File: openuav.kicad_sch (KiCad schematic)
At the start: 73 parts, among them J1 Conn_01x01, J10 Conn_01x01, J11 Conn_01x01, J12 Conn_01x01, J13 Conn_01x01, J14 Conn_01x01, J15 Conn_01x01, J16 Conn_01x01, J17 Conn_01x01, J18 Conn_01x01, J19 Conn_01x01, J2 Conn_01x01, J20 Conn_01x01, J21 Conn_01x01, J22 Conn_01x01, J23 Conn_01x01, J24 Conn_01x01, J25 Conn_01x01, J26 Conn_01x01, J27 Conn_01x01, J28 Conn_01x01, J29 Conn_01x01, J3 Conn_01x01, J30 Conn_01x01, J31 Conn_01x01, J32 Conn_01x01, J33 Conn_01x01, J34 Conn_01x01, J35 Conn_01x01, J36 Conn_01x01, J37 Conn_01x01, J4 Conn_01x01, J5 Conn_01x01, J6 Conn_01x01, J7 Conn_01x01, J8 Conn_01x01, J9 Conn_01x01, J99 USB_C_Receptacle_USB2.0, U1 STM32G431CBUx, U3 LSM6DSR, U4 LPS22HH, U5 TPS54202DDC, U6 W25N01GVZEIG, U7 XC6206P332MR

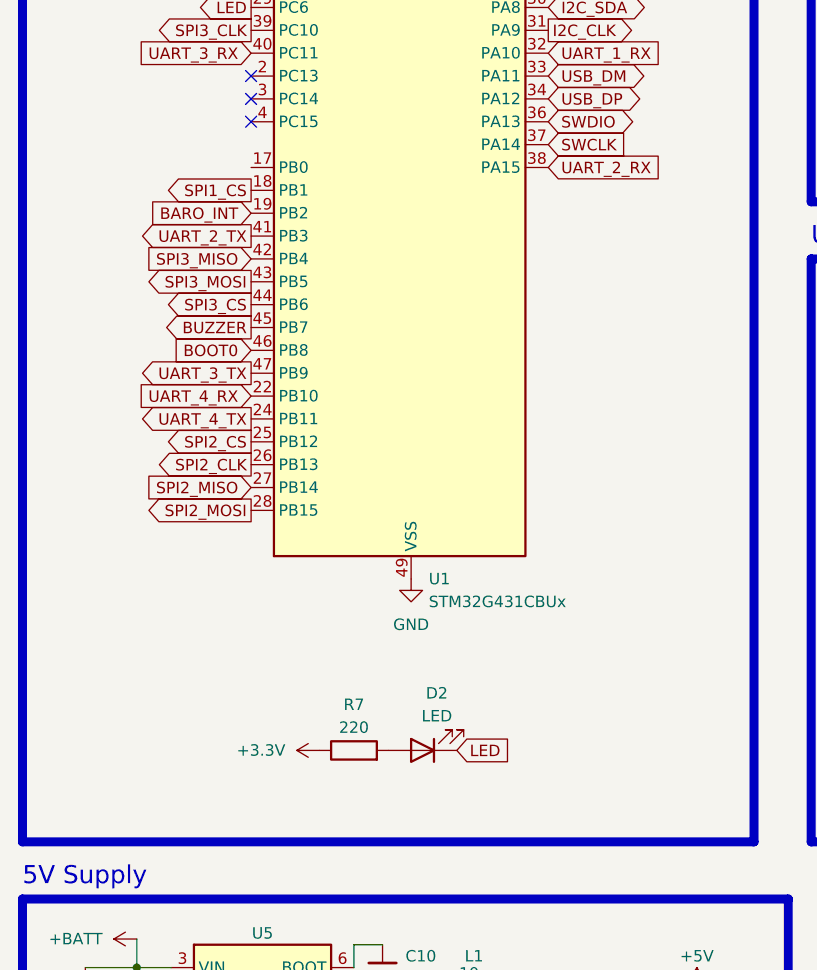
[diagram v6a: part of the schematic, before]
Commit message: update ioc file with all pins, add pulldown on boot0
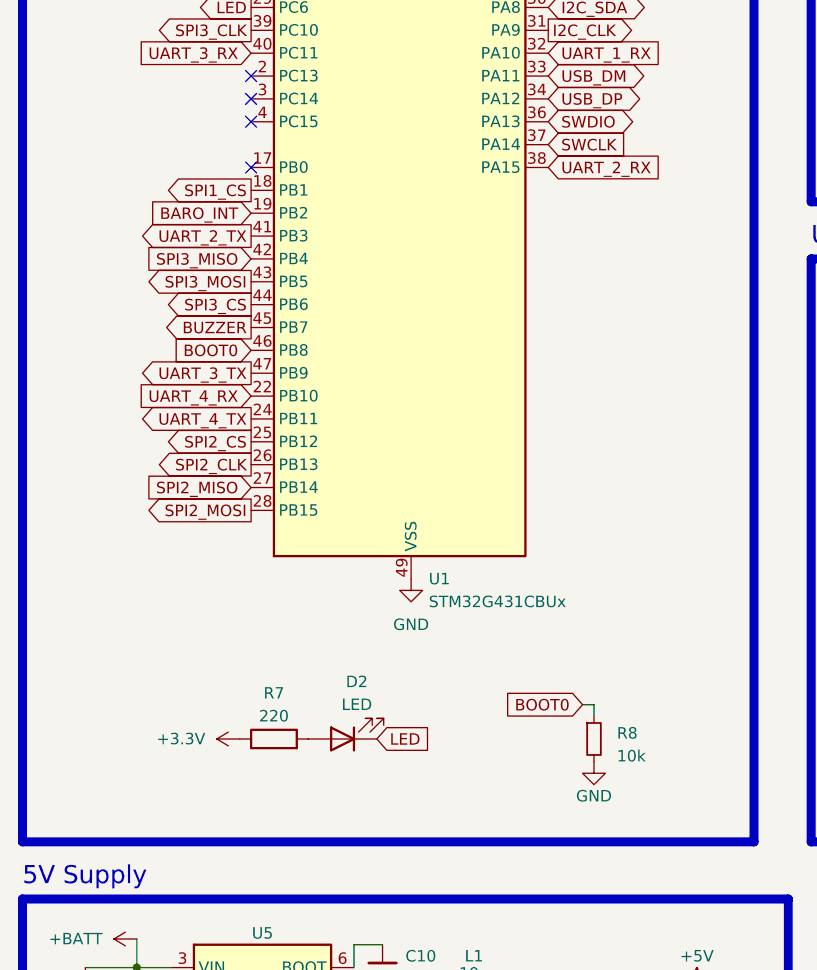
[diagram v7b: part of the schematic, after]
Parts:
- added R8: 10k, Resistor_SMD:R_0402_1005Metric, symbol Device:R_Small
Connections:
- net BOOT0: now also R8.1
- net GND: now also R8.2
- no-connect marks 12 -> 13
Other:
- moved on the sheet: D2, R7
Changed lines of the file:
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@@
   (no_connect (at 41.91 68.58))
   (no_connect (at 113.03 58.42))
+  (no_connect (at 41.91 76.2))
   (no_connect (at 121.92 101.6))
   (no_connect (at 178.435 115.57))
@@
     (stroke (width 0) (type default))
   )
+  (wire (pts (xy 80.01 135.89) (xy 80.01 137.16))
+    (stroke (width 0) (type default))
+  )
   (wire (pts (xy 259.334 175.26) (xy 269.494 175.26))
     (stroke (width 0) (type default))
@@
     (stroke (width 0) (type default))
   )
+  (wire (pts (xy 78.74 135.89) (xy 80.01 135.89))
+    (stroke (width 0) (type default))
+  )
   (wire (pts (xy 29.21 34.29) (xy 34.29 34.29))
     (stroke (width 0) (type default))
@@
     )
   )
-  (global_label "LED" (shape input) (at 64.77 140.97 0) (fields_autoplaced)
+  (global_label "LED" (shape input) (at 55.88 139.7 0) (fields_autoplaced)
     (effects (font (size 1.27 1.27)) (justify left))
-    (property "Intersheetrefs" "${INTERSHEET_REFS}" (at 71.1229 140.97 0)
+    (property "Intersheetrefs" "${INTERSHEET_REFS}" (at 62.2329 139.7 0)
       (effects (font (size 1.27 1.27)) (justify left) hide)
     )
@@
     )
   )
+  (global_label "BOOT0" (shape input) (at 78.74 135.89 180) (fields_autoplaced)
+    (effects (font (size 1.27 1.27)) (justify right))
+    (property "Intersheetrefs" "${INTERSHEET_REFS}" (at 69.7261 135.89 0)
+      (effects (font (size 1.27 1.27)) (justify right) hide)
+    )
+  )
   (global_label "SPI2_MOSI" (shape output) (at 41.91 114.3 180) (fields_autoplaced)
     (effects (font (size 1.27 1.27)) (justify right))
@@
     )
   )
+  (symbol (lib_id "Device:R_Small") (at 80.01 139.7 0) (unit 1)
+    (in_bom yes) (on_board yes) (dnp no) (fields_autoplaced)
+    (property "Reference" "R8" (at 82.55 139.065 0)
+      (effects (font (size 1.27 1.27)) (justify left))
+    )
+    (property "Value" "10k" (at 82.55 141.605 0)
+      (effects (font (size 1.27 1.27)) (justify left))
+    )
+    (property "Footprint" "Resistor_SMD:R_0402_1005Metric" (at 80.01 139.7 0)
+      (effects (font (size 1.27 1.27)) hide)
+    )
+    (property "Datasheet" "~" (at 80.01 139.7 0)
+      (effects (font (size 1.27 1.27)) hide)
+    )
+    (property "LCSC" "C17414" (at 80.01 139.7 0)
+      (effects (font (size 1.27 1.27)) hide)
+    )
+    (pin "1")
+    (pin "2")
+    (instances
+      (project "openuav"
+        (path "/e63e39d7-6ac0-4ffd-8aa3-1841a4541b55"
+          (reference "R8") (unit 1)
+        )
+      )
+    )
+  )
   (symbol (lib_id "power:GND") (at 59.69 121.92 0) (unit 1)
     (in_bom yes) (on_board yes) (dnp no) (fields_autoplaced)
@@
     )
   )
-  (symbol (lib_id "power:+3.3V") (at 49.53 140.97 90) (unit 1)
+  (symbol (lib_id "power:+3.3V") (at 40.64 139.7 90) (unit 1)
     (in_bom yes) (on_board yes) (dnp no)
-    (property "Reference" "#PWR023" (at 53.34 140.97 0)
+    (property "Reference" "#PWR023" (at 44.45 139.7 0)
       (effects (font (size 1.27 1.27)) hide)
     )
-    (property "Value" "+3.3V" (at 45.72 140.97 90)
+    (property "Value" "+3.3V" (at 36.83 139.7 90)
       (effects (font (size 1.27 1.27)) (justify left))
     )
-    (property "Footprint" "" (at 49.53 140.97 0)
+    (property "Footprint" "" (at 40.64 139.7 0)
       (effects (font (size 1.27 1.27)) hide)
     )
-    (property "Datasheet" "" (at 49.53 140.97 0)
+    (property "Datasheet" "" (at 40.64 139.7 0)
       (effects (font (size 1.27 1.27)) hide)
     )
@@
     )
   )
+  (symbol (lib_id "power:GND") (at 80.01 142.24 0) (unit 1)
+    (in_bom yes) (on_board yes) (dnp no)
+    (property "Reference" "#PWR039" (at 80.01 148.59 0)
+      (effects (font (size 1.27 1.27)) hide)
+    )
+    (property "Value" "GND" (at 80.01 146.05 0)
+      (effects (font (size 1.27 1.27)))
+    )
+    (property "Footprint" "" (at 80.01 142.24 0)
+      (effects (font (size 1.27 1.27)) hide)
+    )
+    (property "Datasheet" "" (at 80.01 142.24 0)
+      (effects (font (size 1.27 1.27)) hide)
+    )
+    (pin "1")
+    (instances
+      (project "openuav"
+        (path "/e63e39d7-6ac0-4ffd-8aa3-1841a4541b55"
+          (reference "#PWR039") (unit 1)
+        )
+      )
+    )
+  )
   (symbol (lib_id "Mechanical:MountingHole") (at 257.81 192.532 0) (unit 1)
     (in_bom yes) (on_board yes) (dnp no)
@@
     )
   )
-  (symbol (lib_id "Device:LED") (at 60.96 140.97 180) (unit 1)
+  (symbol (lib_id "Device:LED") (at 52.07 139.7 180) (unit 1)
     (in_bom yes) (on_board yes) (dnp no) (fields_autoplaced)
-    (property "Reference" "D2" (at 62.5475 134.62 0)
+    (property "Reference" "D2" (at 53.6575 133.35 0)
       (effects (font (size 1.27 1.27)))
     )
-    (property "Value" "LED" (at 62.5475 137.16 0)
+    (property "Value" "LED" (at 53.6575 135.89 0)
       (effects (font (size 1.27 1.27)))
     )
-    (property "Footprint" "LED_SMD:LED_0603_1608Metric" (at 60.96 140.97 0)
+    (property "Footprint" "LED_SMD:LED_0603_1608Metric" (at 52.07 139.7 0)
       (effects (font (size 1.27 1.27)) hide)
     )
-    (property "Datasheet" "~" (at 60.96 140.97 0)
+    (property "Datasheet" "~" (at 52.07 139.7 0)
       (effects (font (size 1.27 1.27)) hide)
     )
-    (property "LCSC" "C72041" (at 60.96 140.97 0)
+    (property "LCSC" "C72041" (at 52.07 139.7 0)
       (effects (font (size 1.27 1.27)) hide)
     )
@@
     )
   )
-  (symbol (lib_id "Device:R") (at 53.34 140.97 90) (unit 1)
+  (symbol (lib_id "Device:R") (at 44.45 139.7 90) (unit 1)
     (in_bom yes) (on_board yes) (dnp no) (fields_autoplaced)
-    (property "Reference" "R7" (at 53.34 135.89 90)
+    (property "Reference" "R7" (at 44.45 134.62 90)
       (effects (font (size 1.27 1.27)))
     )
-    (property "Value" "220" (at 53.34 138.43 90)
+    (property "Value" "220" (at 44.45 137.16 90)
       (effects (font (size 1.27 1.27)))
     )
-    (property "Footprint" "Resistor_SMD:R_0805_2012Metric" (at 53.34 142.748 90)
+    (property "Footprint" "Resistor_SMD:R_0805_2012Metric" (at 44.45 141.478 90)
       (effects (font (size 1.27 1.27)) hide)
     )
-    (property "Datasheet" "~" (at 53.34 140.97 0)
+    (property "Datasheet" "~" (at 44.45 139.7 0)
       (effects (font (size 1.27 1.27)) hide)
     )
-    (property "LCSC" "C17557" (at 53.34 140.97 90)
+    (property "LCSC" "C17557" (at 44.45 139.7 90)
       (effects (font (size 1.27 1.27)) hide)
     )

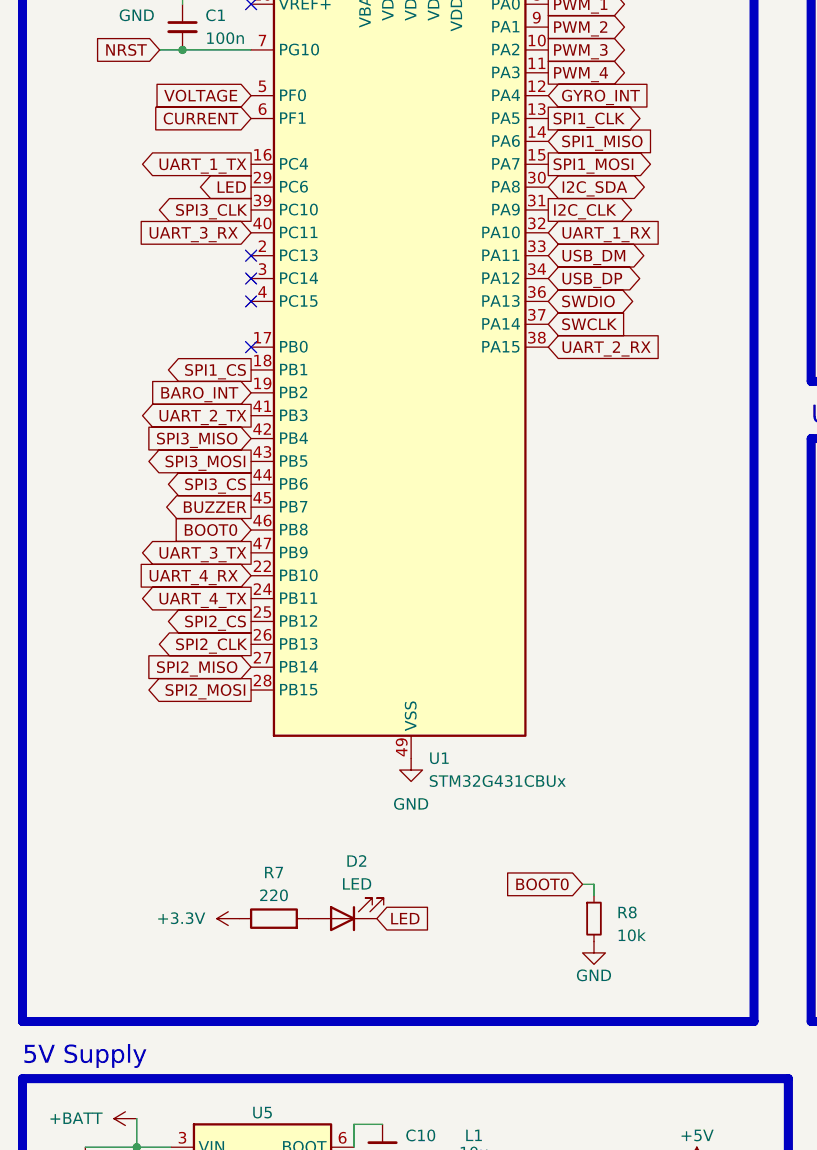
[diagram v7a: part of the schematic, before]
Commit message: add note about TT pin
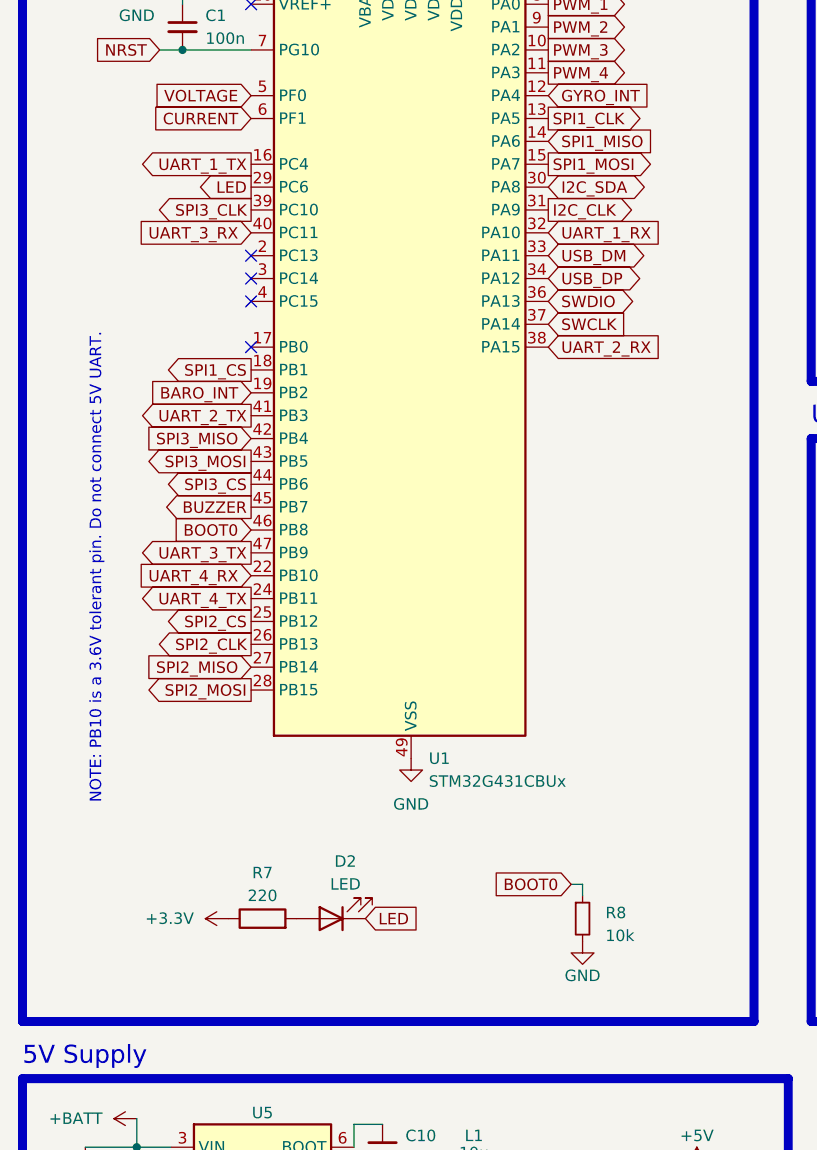
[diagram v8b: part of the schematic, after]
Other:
- note added: "NOTE: PB10 is a 3.6V tolerant pin. Do not connect 5V UART."
- moved on the sheet: D2, R7, R8
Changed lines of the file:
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@@
     (stroke (width 0) (type default))
   )
-  (wire (pts (xy 80.01 135.89) (xy 80.01 137.16))
+  (wire (pts (xy 78.74 135.89) (xy 78.74 137.16))
     (stroke (width 0) (type default))
   )
@@
     (stroke (width 0) (type default))
   )
-  (wire (pts (xy 78.74 135.89) (xy 80.01 135.89))
+  (wire (pts (xy 77.47 135.89) (xy 78.74 135.89))
     (stroke (width 0) (type default))
   )
@@
     (effects (font (size 2 2)) (justify left bottom))
   )
+  (text "NOTE: PB10 is a 3.6V tolerant pin. Do not connect 5V UART."
+    (at 25.4 127 90)
+    (effects (font (size 1.27 1.27)) (justify left bottom))
+  )
   (text "Flash" (at 161.29 85.09 0)
     (effects (font (size 2 2)) (justify left bottom))
@@
     )
   )
-  (global_label "LED" (shape input) (at 55.88 139.7 0) (fields_autoplaced)
+  (global_label "LED" (shape input) (at 54.61 139.7 0) (fields_autoplaced)
     (effects (font (size 1.27 1.27)) (justify left))
-    (property "Intersheetrefs" "${INTERSHEET_REFS}" (at 62.2329 139.7 0)
+    (property "Intersheetrefs" "${INTERSHEET_REFS}" (at 60.9629 139.7 0)
       (effects (font (size 1.27 1.27)) (justify left) hide)
     )
@@
     )
   )
-  (global_label "BOOT0" (shape input) (at 78.74 135.89 180) (fields_autoplaced)
+  (global_label "BOOT0" (shape input) (at 77.47 135.89 180) (fields_autoplaced)
     (effects (font (size 1.27 1.27)) (justify right))
-    (property "Intersheetrefs" "${INTERSHEET_REFS}" (at 69.7261 135.89 0)
+    (property "Intersheetrefs" "${INTERSHEET_REFS}" (at 68.4561 135.89 0)
       (effects (font (size 1.27 1.27)) (justify right) hide)
     )
@@
     )
   )
-  (symbol (lib_id "Device:R_Small") (at 80.01 139.7 0) (unit 1)
+  (symbol (lib_id "Device:R_Small") (at 78.74 139.7 0) (unit 1)
     (in_bom yes) (on_board yes) (dnp no) (fields_autoplaced)
-    (property "Reference" "R8" (at 82.55 139.065 0)
+    (property "Reference" "R8" (at 81.28 139.065 0)
       (effects (font (size 1.27 1.27)) (justify left))
     )
-    (property "Value" "10k" (at 82.55 141.605 0)
+    (property "Value" "10k" (at 81.28 141.605 0)
       (effects (font (size 1.27 1.27)) (justify left))
     )
-    (property "Footprint" "Resistor_SMD:R_0402_1005Metric" (at 80.01 139.7 0)
+    (property "Footprint" "Resistor_SMD:R_0402_1005Metric" (at 78.74 139.7 0)
       (effects (font (size 1.27 1.27)) hide)
     )
-    (property "Datasheet" "~" (at 80.01 139.7 0)
+    (property "Datasheet" "~" (at 78.74 139.7 0)
       (effects (font (size 1.27 1.27)) hide)
     )
-    (property "LCSC" "C17414" (at 80.01 139.7 0)
+    (property "LCSC" "C17414" (at 78.74 139.7 0)
       (effects (font (size 1.27 1.27)) hide)
     )
@@
     )
   )
-  (symbol (lib_id "power:+3.3V") (at 40.64 139.7 90) (unit 1)
+  (symbol (lib_id "power:+3.3V") (at 39.37 139.7 90) (unit 1)
     (in_bom yes) (on_board yes) (dnp no)
-    (property "Reference" "#PWR023" (at 44.45 139.7 0)
+    (property "Reference" "#PWR023" (at 43.18 139.7 0)
       (effects (font (size 1.27 1.27)) hide)
     )
-    (property "Value" "+3.3V" (at 36.83 139.7 90)
+    (property "Value" "+3.3V" (at 35.56 139.7 90)
       (effects (font (size 1.27 1.27)) (justify left))
     )
-    (property "Footprint" "" (at 40.64 139.7 0)
+    (property "Footprint" "" (at 39.37 139.7 0)
       (effects (font (size 1.27 1.27)) hide)
     )
-    (property "Datasheet" "" (at 40.64 139.7 0)
+    (property "Datasheet" "" (at 39.37 139.7 0)
       (effects (font (size 1.27 1.27)) hide)
     )
@@
     )
   )
-  (symbol (lib_id "power:GND") (at 80.01 142.24 0) (unit 1)
+  (symbol (lib_id "power:GND") (at 78.74 142.24 0) (unit 1)
     (in_bom yes) (on_board yes) (dnp no)
-    (property "Reference" "#PWR039" (at 80.01 148.59 0)
+    (property "Reference" "#PWR039" (at 78.74 148.59 0)
       (effects (font (size 1.27 1.27)) hide)
     )
-    (property "Value" "GND" (at 80.01 146.05 0)
+    (property "Value" "GND" (at 78.74 146.05 0)
       (effects (font (size 1.27 1.27)))
     )
-    (property "Footprint" "" (at 80.01 142.24 0)
+    (property "Footprint" "" (at 78.74 142.24 0)
       (effects (font (size 1.27 1.27)) hide)
     )
-    (property "Datasheet" "" (at 80.01 142.24 0)
+    (property "Datasheet" "" (at 78.74 142.24 0)
       (effects (font (size 1.27 1.27)) hide)
     )
@@
     )
   )
-  (symbol (lib_id "Device:LED") (at 52.07 139.7 180) (unit 1)
+  (symbol (lib_id "Device:LED") (at 50.8 139.7 180) (unit 1)
     (in_bom yes) (on_board yes) (dnp no) (fields_autoplaced)
-    (property "Reference" "D2" (at 53.6575 133.35 0)
+    (property "Reference" "D2" (at 52.3875 133.35 0)
       (effects (font (size 1.27 1.27)))
     )
-    (property "Value" "LED" (at 53.6575 135.89 0)
+    (property "Value" "LED" (at 52.3875 135.89 0)
       (effects (font (size 1.27 1.27)))
     )
-    (property "Footprint" "LED_SMD:LED_0603_1608Metric" (at 52.07 139.7 0)
+    (property "Footprint" "LED_SMD:LED_0603_1608Metric" (at 50.8 139.7 0)
       (effects (font (size 1.27 1.27)) hide)
     )
-    (property "Datasheet" "~" (at 52.07 139.7 0)
+    (property "Datasheet" "~" (at 50.8 139.7 0)
       (effects (font (size 1.27 1.27)) hide)
     )
-    (property "LCSC" "C72041" (at 52.07 139.7 0)
+    (property "LCSC" "C72041" (at 50.8 139.7 0)
       (effects (font (size 1.27 1.27)) hide)
     )
@@
     )
   )
-  (symbol (lib_id "Device:R") (at 44.45 139.7 90) (unit 1)
+  (symbol (lib_id "Device:R") (at 43.18 139.7 90) (unit 1)
     (in_bom yes) (on_board yes) (dnp no) (fields_autoplaced)
-    (property "Reference" "R7" (at 44.45 134.62 90)
+    (property "Reference" "R7" (at 43.18 134.62 90)
       (effects (font (size 1.27 1.27)))
     )
-    (property "Value" "220" (at 44.45 137.16 90)
+    (property "Value" "220" (at 43.18 137.16 90)
       (effects (font (size 1.27 1.27)))
     )
-    (property "Footprint" "Resistor_SMD:R_0805_2012Metric" (at 44.45 141.478 90)
+    (property "Footprint" "Resistor_SMD:R_0805_2012Metric" (at 43.18 141.478 90)
       (effects (font (size 1.27 1.27)) hide)
     )
-    (property "Datasheet" "~" (at 44.45 139.7 0)
+    (property "Datasheet" "~" (at 43.18 139.7 0)
       (effects (font (size 1.27 1.27)) hide)
     )
-    (property "LCSC" "C17557" (at 44.45 139.7 90)
+    (property "LCSC" "C17557" (at 43.18 139.7 90)
       (effects (font (size 1.27 1.27)) hide)
     )
